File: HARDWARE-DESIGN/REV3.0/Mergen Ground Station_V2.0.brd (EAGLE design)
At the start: 83.8 x 55.9 mm, 75 parts, among them J2 CON-SD-CARD_MICROSD-2908-05, J4 U.FL, U13 L86, U15 AMS1117-5V, U16 AMS1117-3.3, X2 JST-XH-04-PIN-LONG-PAD, Y1 ABMM2-8.000MHZ-E2-T

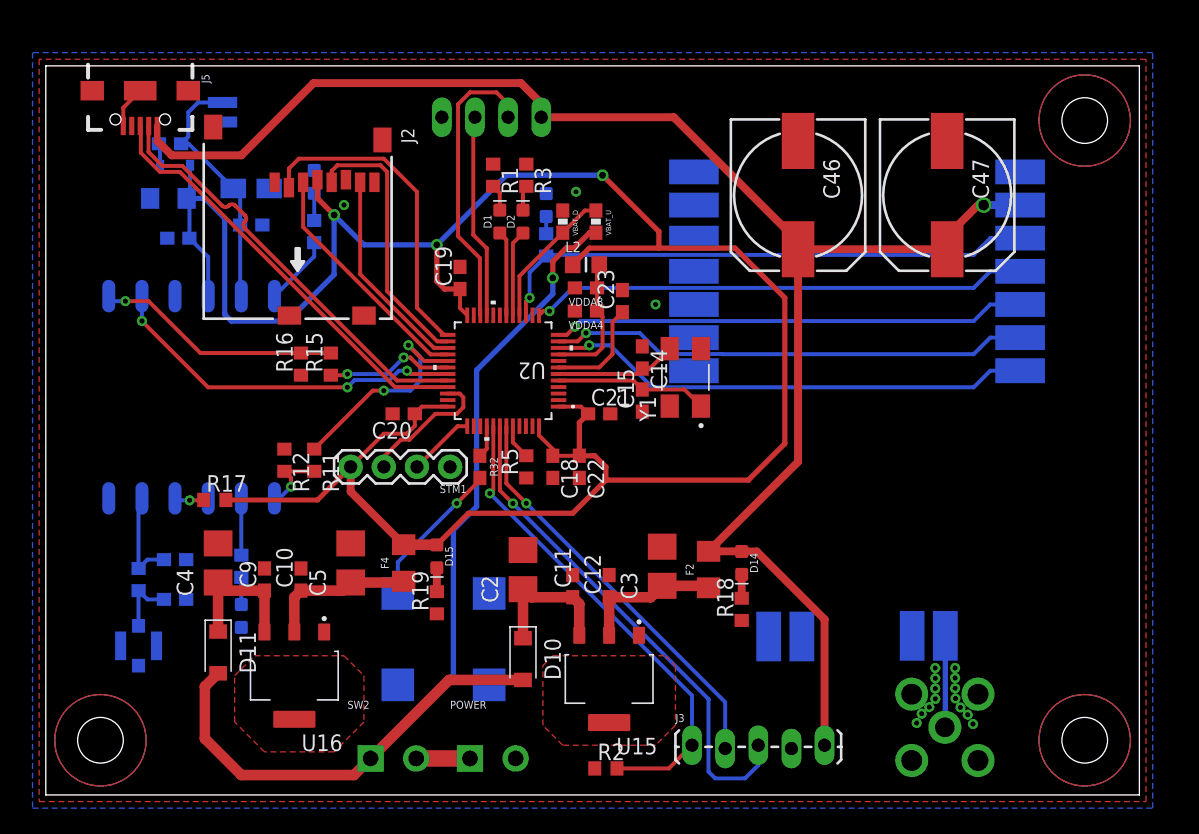
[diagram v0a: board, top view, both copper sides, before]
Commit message: new buzzer was added
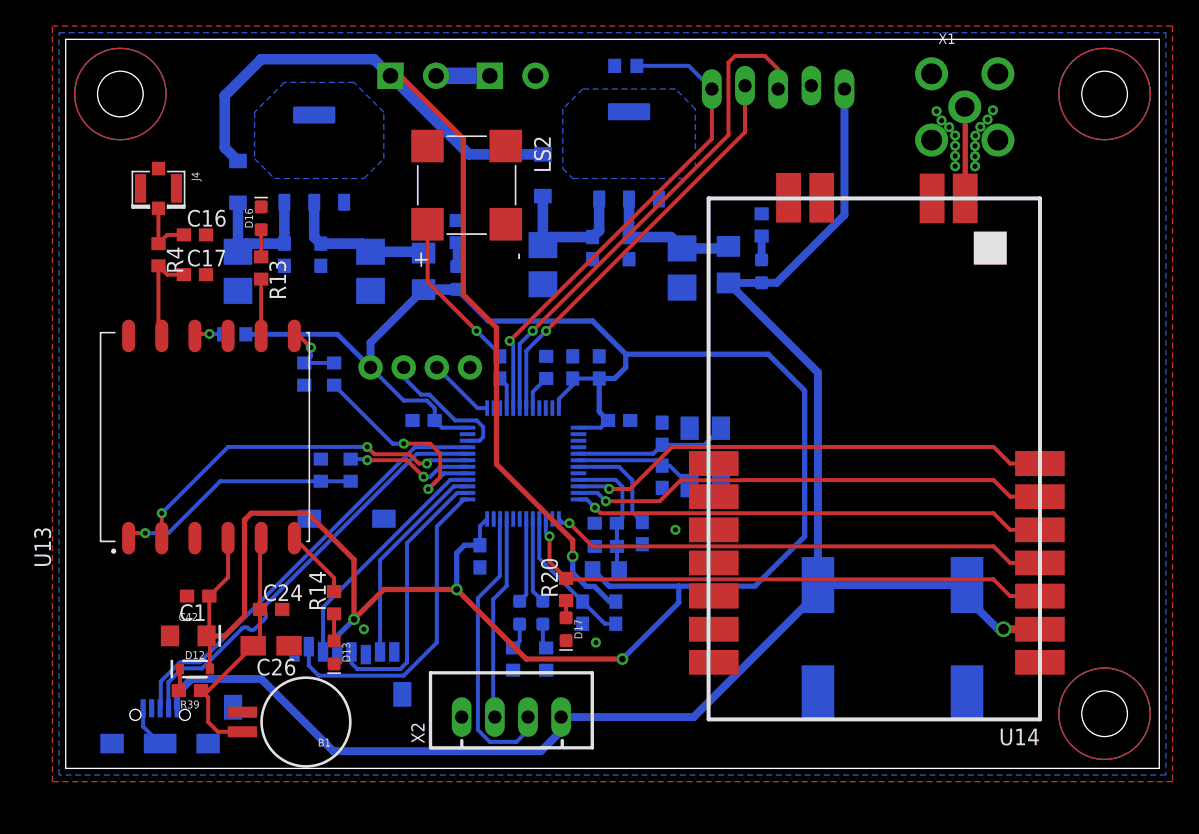
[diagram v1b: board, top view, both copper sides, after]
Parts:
- removed LS1: CMT-8530S-SMT, SMT-BUZZER:CUI_CMT-8530S-SMT
- added LS2: CMT-7525S-SMT, CMT-7525S-SMT:CUI_CMT-7525S-SMT
- moved R2 53.9 mm to (44.5, 55.9), flipped to the bottom, turned to 180 degrees
- moved POWER 52.3 mm to (34.0, 55.1), flipped to the bottom, turned to 180 degrees
- moved SW2 52.3 mm to (26.4, 55.1), flipped to the bottom, turned to 180 degrees
- moved J3 50.3 mm to (51.1, 54.1), flipped to the bottom, turned to 180 degrees
- moved J5 50.1 mm to (8.76, 3.94), flipped to the bottom, turned to 90 degrees
- moved X1 47.6 mm to (70.4, 52.7), flipped to the top, turned to 0 degrees
- moved B1 46.8 mm to (19.9, 5.59), flipped to the top, turned to 180 degrees
- moved X2 46.0 mm to (35.7, 5.97), flipped to the top, turned to 0 degrees
- moved J2 43.7 mm to (20.8, 7.11), flipped to the bottom, turned to 0 degrees
- moved R39 41.9 mm to (11.0, 8.00), flipped to the top, turned to 180 degrees
- moved U15 40.2 mm to (44.7, 49.0), flipped to the bottom, turned to 0 degrees
- moved U16 39.7 mm to (20.6, 48.8), flipped to the bottom, turned to 0 degrees
- moved D12 38.6 mm to (11.4, 9.65), flipped to the top, turned to 0 degrees
- moved D10 37.1 mm to (38.1, 47.5), flipped to the bottom, turned to 90 degrees
- moved R1 37.1 mm to (35.8, 10.4), flipped to the bottom, turned to 90 degrees
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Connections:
- net GND: now also LS2.N; no longer LS1.N
- net N$4: now also LS2.P; no longer LS1.P
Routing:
- net N$4: track 11.5 -> 12.4 mm
- added copper zone on layer 16, net HT
- added copper zone on layer 16, net HT2
- removed copper zone on layer 1, net HT
- removed copper zone on layer 1, net HT2
